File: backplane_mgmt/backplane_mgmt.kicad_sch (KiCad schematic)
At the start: 1 part, among them J101 LineOut

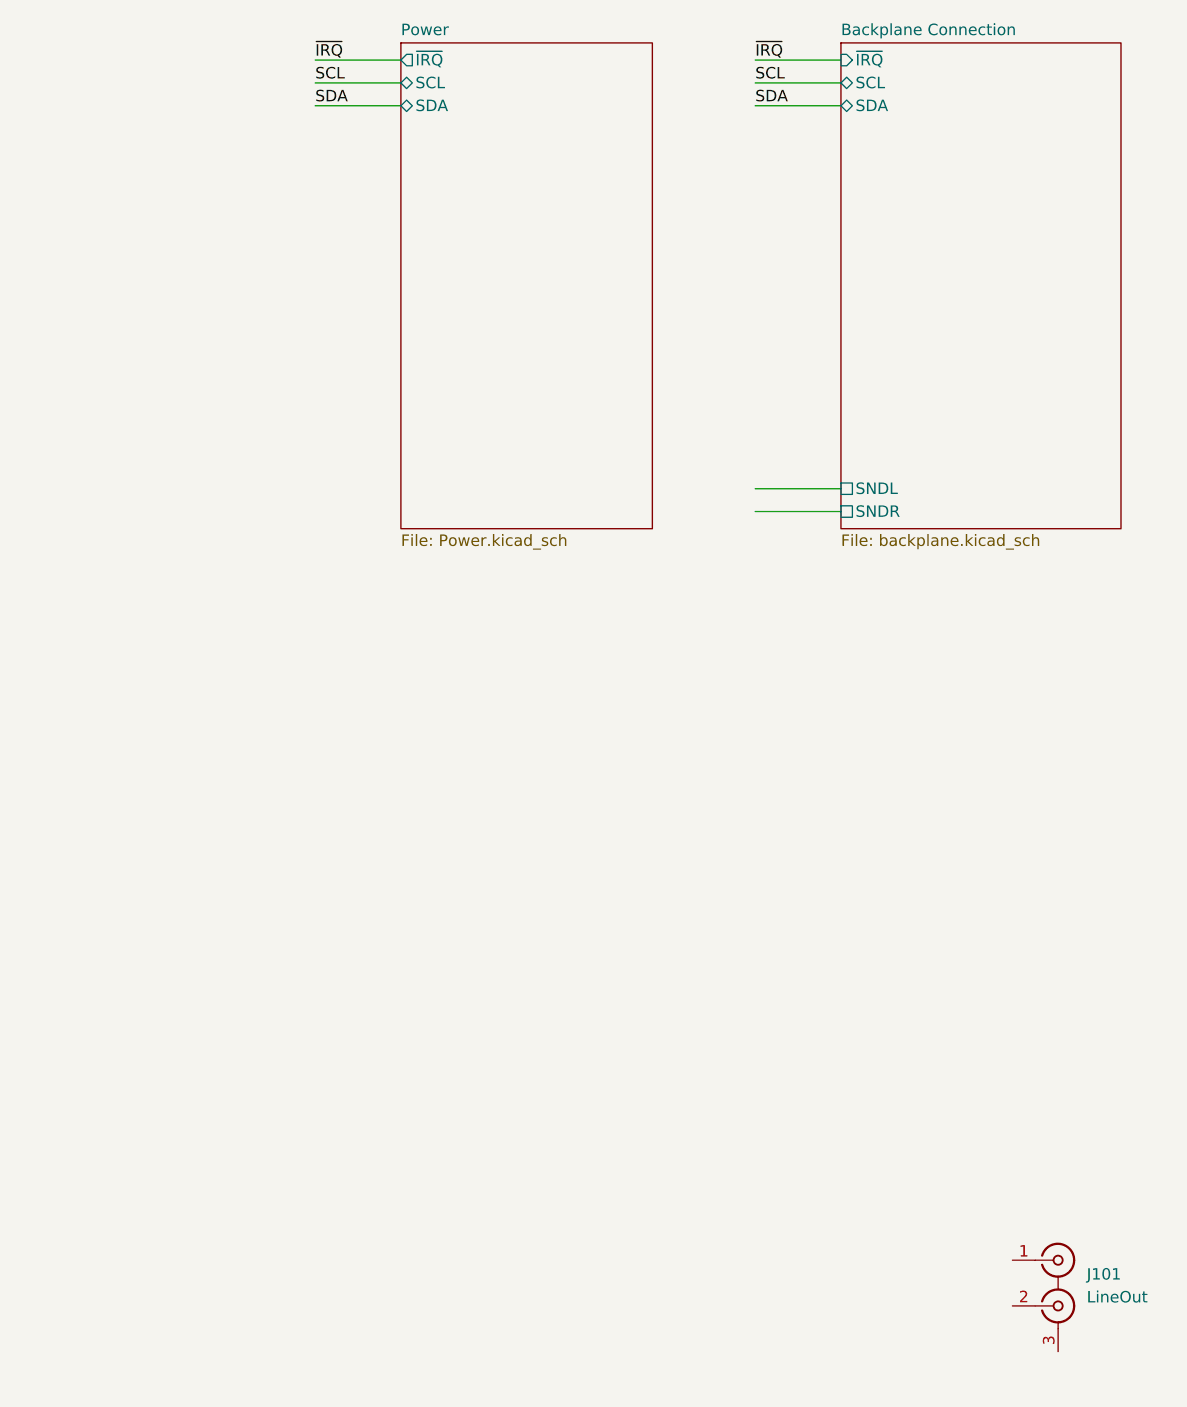
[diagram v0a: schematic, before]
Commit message: Routed backplane mgmt board
- Finished routing of the complete backplane management board; it
  doesn't do much other than provide power (with monitoring) and an
  audio output (with volume control) from the backplane.

  Originally this was gonna have a display but there's no space on the
  front panel for that.
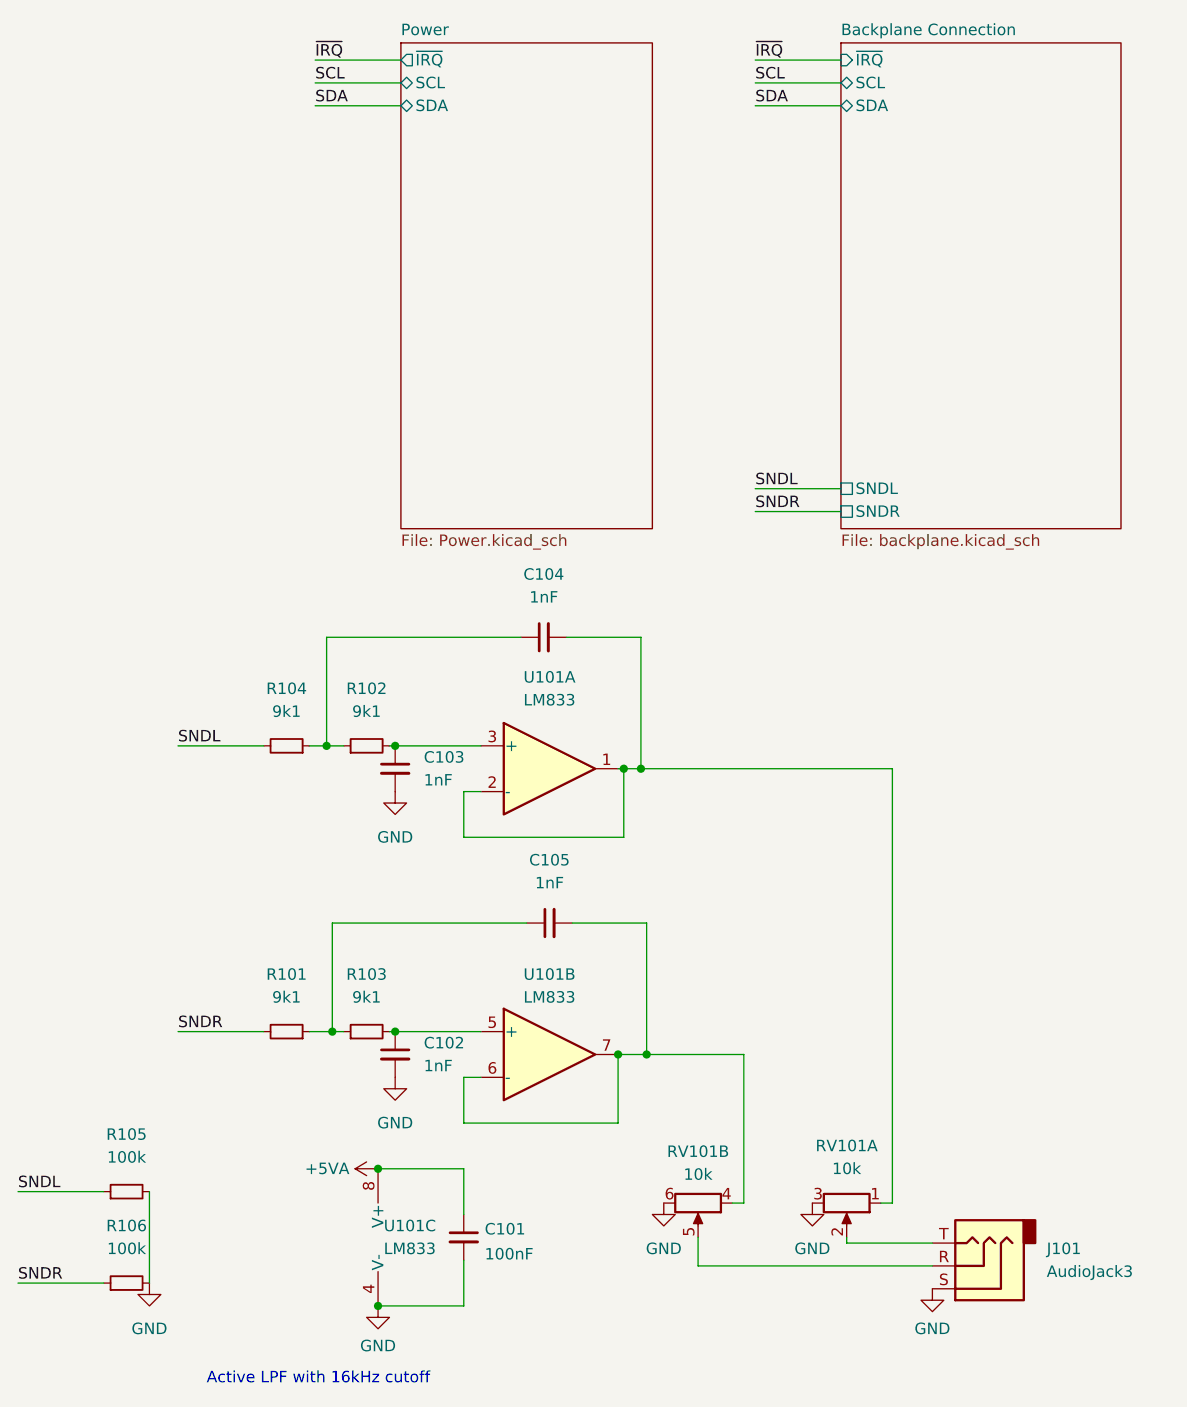
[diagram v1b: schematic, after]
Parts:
- removed J101: LineOut, symbol Connector:Conn_Coaxial_x2
- added C101: 100nF, Capacitor_SMD:C_0805_2012Metric, symbol Device:C_Small
- added C102, C103, C104, C105: 1nF, Capacitor_THT:C_Rect_L7.2mm_W2.5mm_P5.00mm_FKS2_FKP2_MKS2_MKP2, symbol Device:C_Small
- added J101: AudioJack3, Connector_Audio:Jack_3.5mm_CUI_SJ1-3533NG_Horizontal, symbol Connector:AudioJack3
- added R101, R102, R103, R104: 9k1, Resistor_SMD:R_0805_2012Metric, symbol Device:R_Small
- added R105, R106: 100k, Resistor_SMD:R_0805_2012Metric, symbol Device:R_Small
- added RV101: 10k, Potentiometer_THT:Potentiometer_Alps_RK097_Dual_Horizontal, symbol Device:R_Potentiometer_Dual_Separate
- added U101: LM833, Package_DIP:DIP-8_W7.62mm_Socket, symbol Amplifier_Operational:LM2904
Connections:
- new net: C105.1, R101.1, R103.1
- new net: C105.2, RV101.4, U101.6 (-), U101.7
- new net: C104.1, R102.1, R104.1
- new net: C104.2, RV101.1, U101.1, U101.2 (-)
- new net: J101.R, RV101.5
- new net: C102.1, R103.2, U101.5 (+)
- new net: C103.1, R102.2, U101.3 (+)
- new net: J101.T, RV101.2
- new net +5VA: C101.1, U101.8 (V+)
- new net GND: C101.2, C102.2, C103.2, J101.S, R105.2, R106.2, RV101.3, RV101.6, U101.4 (V-)
- new net SNDL: R104.2, R105.1
- new net SNDR: R101.2, R106.1
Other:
- note added: "Active LPF with 16kHz cutoff"

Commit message: Minor tweaks to all boards
- Moved around some traces on the 68000 CPU card for prettiness

- Added a connector on the backplane to provide +5V/+12V without a
  management card installed (for testing)
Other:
- company: (none) -> Tristan Seifert
- title: (none) -> Backplane Management and Power
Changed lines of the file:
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@@
 (kicad_sch (version 20211123) (generator eeschema)
   (paper "A4")
+  (title_block
+    (title "Backplane Management and Power")
+    (date "2022-01-09")
+    (rev "1")
+    (company "Tristan Seifert")
+  )
   (junction (at 225.425 96.52) (diameter 0) (color 0 0 0 0)
   )
